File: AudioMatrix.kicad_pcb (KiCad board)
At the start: 2 copper layers, 100 x 100 mm, 124 parts, among them J1 AMP3, J2 AMP1, J3 AMP2, J4 Audio In, J5 3V3, J6 5V, J7 GND, J8 IO, J9 ESP, U1 PT2258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

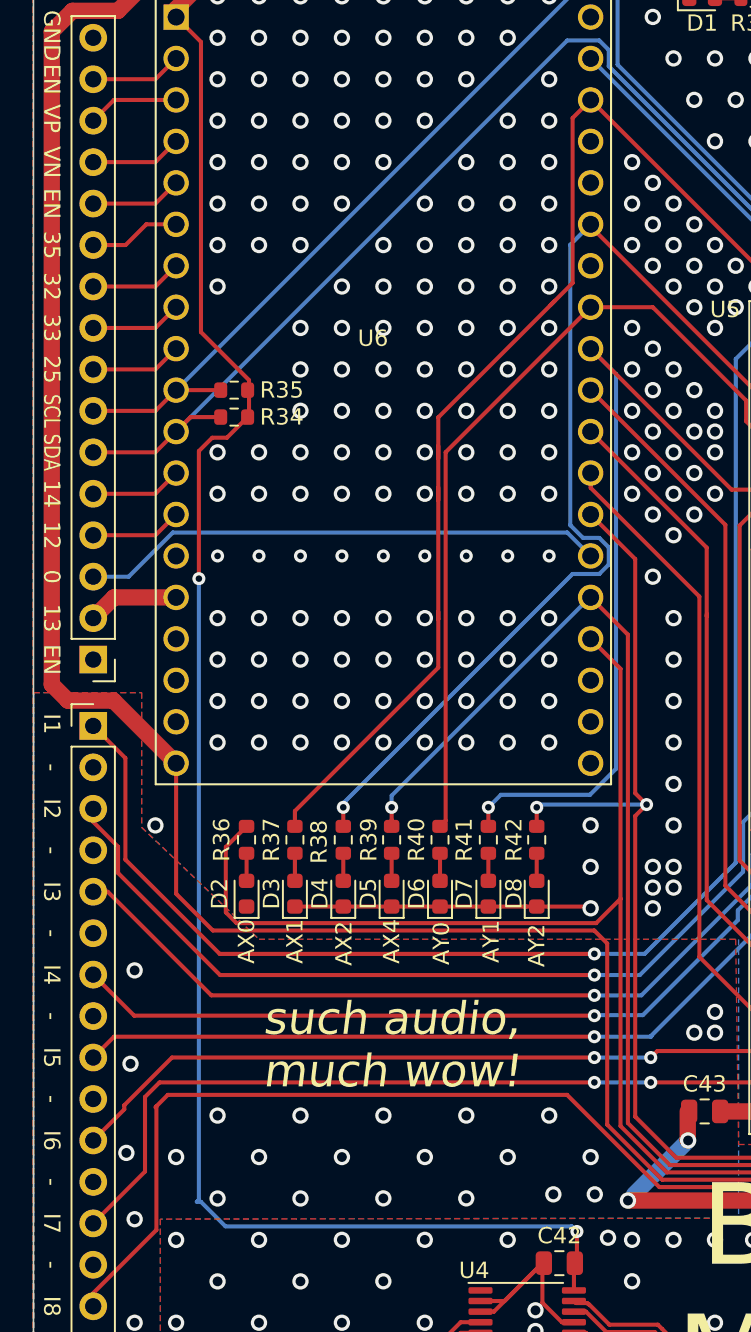
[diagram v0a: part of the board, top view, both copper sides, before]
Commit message: Removed LEDs
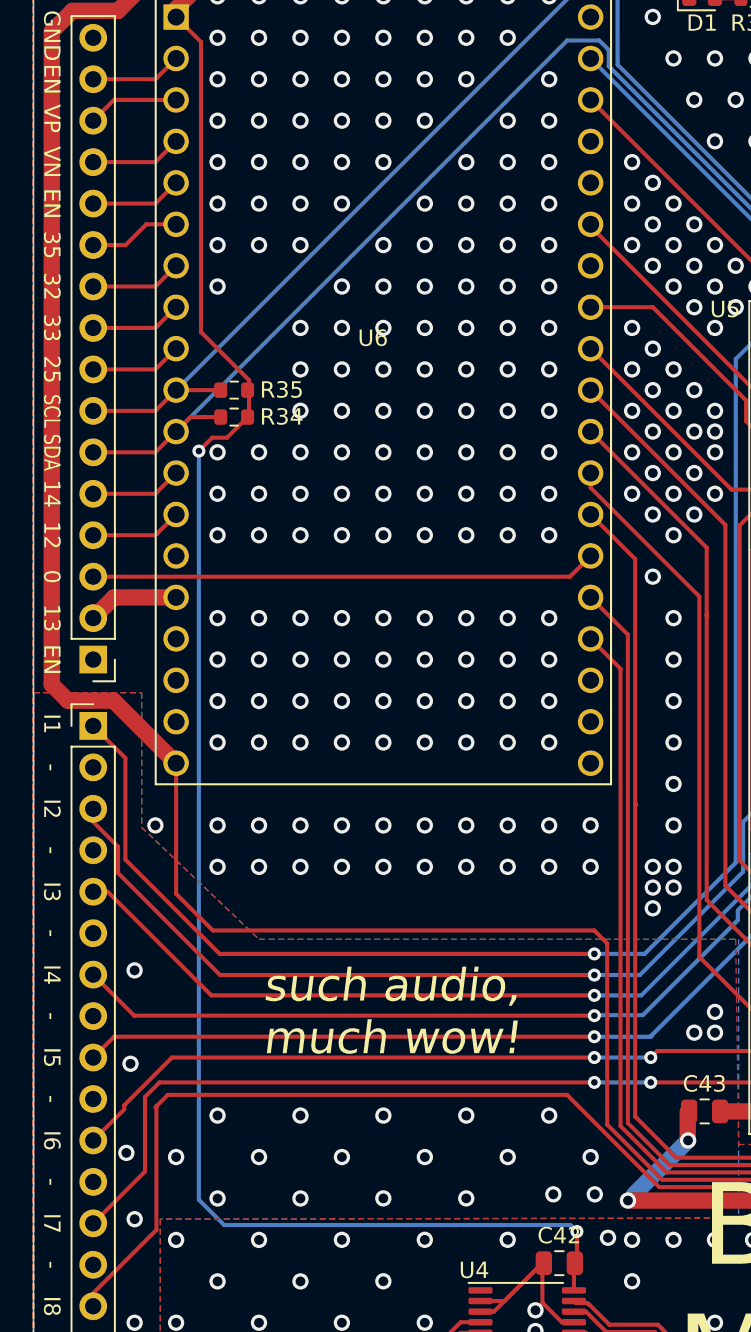
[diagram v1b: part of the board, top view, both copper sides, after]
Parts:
- removed D2, D3, D4, D5: LED_R, Diode_SMD:D_0603_1608Metric
- removed D6, D7, D8: LED_G, Diode_SMD:D_0603_1608Metric
- removed R36, R37, R38, R39, R40, R41, R42: 510, Resistor_SMD:R_0603_1608Metric
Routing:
- net /AX1: track 76.2 -> 21.8 mm
- net /AX2: track 62.4 -> 15.8 mm, vias 1 -> 0
- net /AY1: track 51.0 -> 14.6 mm, vias 1 -> 0
- net /AY0: track 51.1 -> 15.4 mm
- net /AX0: track 104.7 -> 73.8 mm
- net /AX3: track 90.8 -> 71.3 mm, vias 1 -> 0
- net GND: track 206.3 -> 188.3 mm, vias 387 -> 395
- net /AY2: track 73.4 -> 64.8 mm, vias 2 -> 0
- net Net-(D8-Pad2): track 1.69 -> 0.00 mm
- net Net-(D7-Pad2): track 1.69 -> 0.00 mm
- net Net-(D6-Pad2): track 1.69 -> 0.00 mm
- net Net-(D5-Pad2): track 1.69 -> 0.00 mm
- net Net-(D4-Pad2): track 1.69 -> 0.00 mm
- net Net-(D3-Pad2): track 1.69 -> 0.00 mm
- net Net-(D2-Pad2): track 1.69 -> 0.00 mm
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
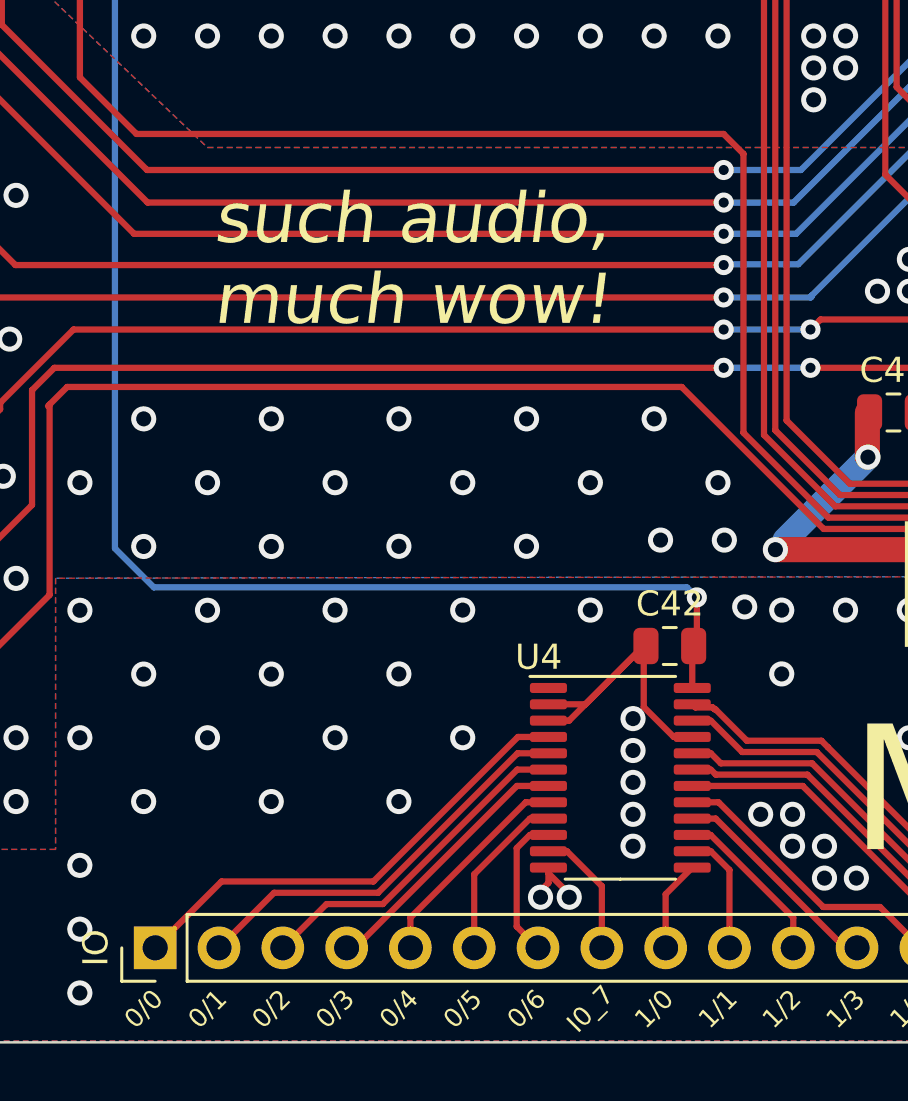
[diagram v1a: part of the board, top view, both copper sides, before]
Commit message: Replaced IO expander
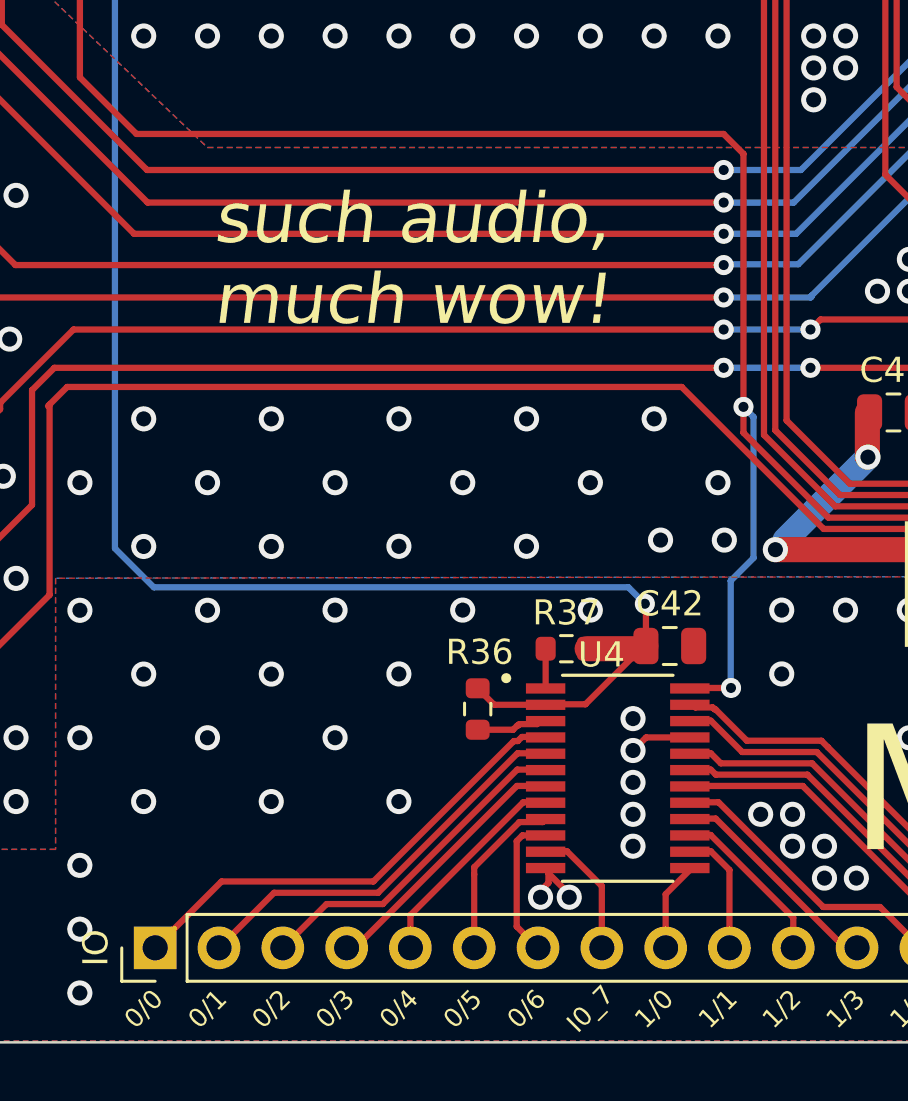
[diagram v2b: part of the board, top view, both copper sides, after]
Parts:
- added R36: 100k, Resistor_SMD:R_0603_1608Metric, F.Cu at (124.6, 136.8)
- added R37: 100k, Resistor_SMD:R_0603_1608Metric, F.Cu at (128.2, 134.4)
- U4: value PCA9555PW -> TCA6416APWR; footprint Package_SO:TSSOP-24_4.4x7.8mm_P0.65mm -> SOP65P640X120-24N:SOP65P640X120-24N
- moved U4 0.11 mm to (130.2, 139.5)
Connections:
- C42 pad 1: GND -> +3V3
- C42 pad 2: /3V3 -> GND
- J5 pad 2: /3V3 -> +3V3
- R33 pad 1: /3V3 -> +3V3
- R34 pad 2: /3V3 -> +3V3
- R35 pad 2: /3V3 -> +3V3
- U4 pad 2: GND -> +3V3
- U4 pad 24: /3V3 -> +5V
- U4 pad 3: GND -> Net-(R36-Pad2)
- U6 pad 1: /3V3 -> +3V3
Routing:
- net +3V3: track 0.00 -> 150.7 mm, vias 0 -> 2
- net /3V3: track 144.5 -> 0.00 mm, vias 2 -> 0
- net +5V: track 234.2 -> 247.6 mm, vias 0 -> 2
- net GND: track 188.3 -> 177.2 mm, vias 395 -> 393
- net Net-(R36-Pad2): track 0.00 -> 2.58 mm
- net Net-(R37-Pad1): track 0.00 -> 1.58 mm
- net /IO0_5: track 6.80 -> 7.58 mm
- net /IO0_6: track 5.80 -> 6.58 mm

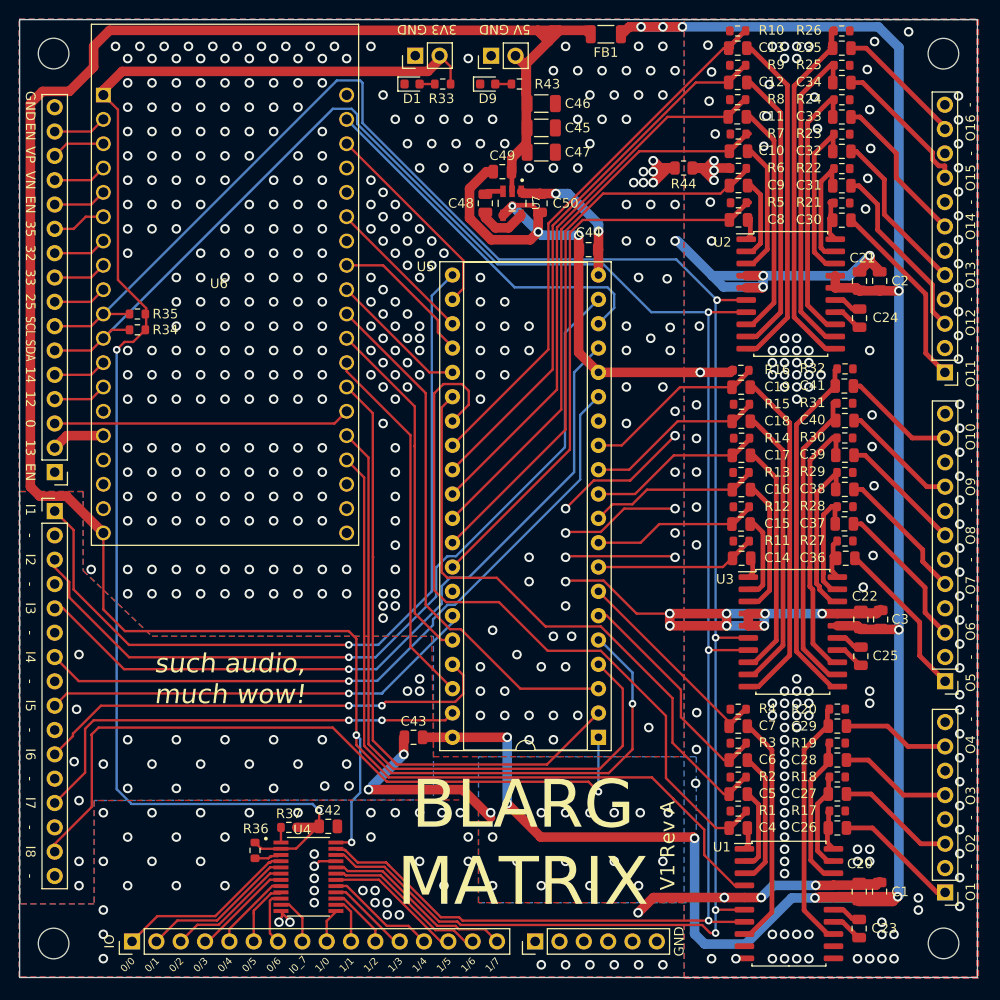
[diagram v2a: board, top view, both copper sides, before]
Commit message: Fixed output cap design
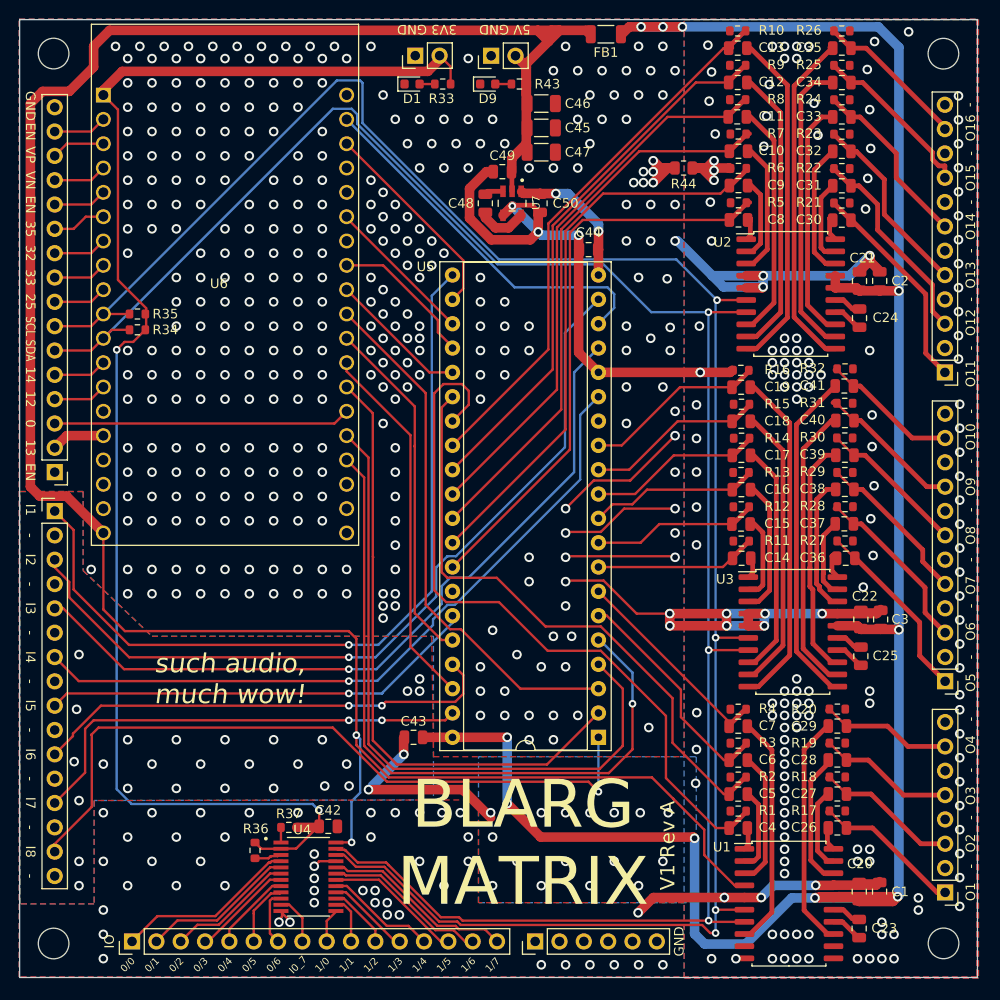
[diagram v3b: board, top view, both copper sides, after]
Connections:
- R17 pad 1: Net-(C26-Pad2) -> Net-(C26-Pad1)
- R18 pad 1: Net-(C27-Pad2) -> Net-(C27-Pad1)
- R19 pad 1: Net-(C28-Pad2) -> Net-(C28-Pad1)
- R20 pad 1: Net-(C29-Pad2) -> Net-(C29-Pad1)
- R21 pad 1: Net-(C30-Pad2) -> Net-(C30-Pad1)
- R22 pad 1: Net-(C31-Pad2) -> Net-(C31-Pad1)
- R23 pad 1: Net-(C32-Pad2) -> Net-(C32-Pad1)
- R24 pad 1: Net-(C33-Pad2) -> Net-(C33-Pad1)
- R25 pad 1: Net-(C34-Pad2) -> Net-(C34-Pad1)
- R26 pad 1: Net-(C35-Pad2) -> Net-(C35-Pad1)
- R27 pad 1: Net-(C36-Pad2) -> Net-(C36-Pad1)
- R28 pad 1: Net-(C37-Pad2) -> Net-(C37-Pad1)
- R29 pad 1: Net-(C38-Pad2) -> Net-(C38-Pad1)
- R30 pad 1: Net-(C39-Pad2) -> Net-(C39-Pad1)
- R31 pad 1: Net-(C40-Pad2) -> Net-(C40-Pad1)
- R32 pad 1: Net-(C41-Pad2) -> Net-(C41-Pad1)
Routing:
- net Net-(C37-Pad2): track 12.5 -> 8.37 mm
- net Net-(C31-Pad2): track 12.4 -> 8.68 mm
- net Net-(C32-Pad2): track 17.7 -> 14.2 mm
- net Net-(C35-Pad2): track 39.1 -> 35.6 mm
- net Net-(C38-Pad2): track 17.5 -> 14.6 mm
- net Net-(C39-Pad2): track 28.0 -> 25.1 mm
- net Net-(C37-Pad1): track 15.7 -> 18.5 mm
- net Net-(C41-Pad1): track 11.7 -> 14.5 mm
- net Net-(C33-Pad2): track 28.1 -> 25.4 mm
- net Net-(C40-Pad1): track 12.3 -> 15.0 mm
- net Net-(C31-Pad1): track 18.9 -> 21.6 mm
- net Net-(C26-Pad1): track 13.0 -> 15.7 mm
- net Net-(C29-Pad1): track 11.1 -> 13.8 mm
- net Net-(C27-Pad1): track 12.4 -> 15.1 mm
- net Net-(C28-Pad1): track 11.7 -> 14.4 mm
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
